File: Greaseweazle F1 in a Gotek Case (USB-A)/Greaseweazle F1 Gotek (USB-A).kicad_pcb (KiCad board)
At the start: 2 copper layers, 111.6 x 68.1 mm, 48 parts, among them CN1 FLOPPY, J1 USB A, J2 Floppy Power, J3 Programming Port, U1 Blue Pill

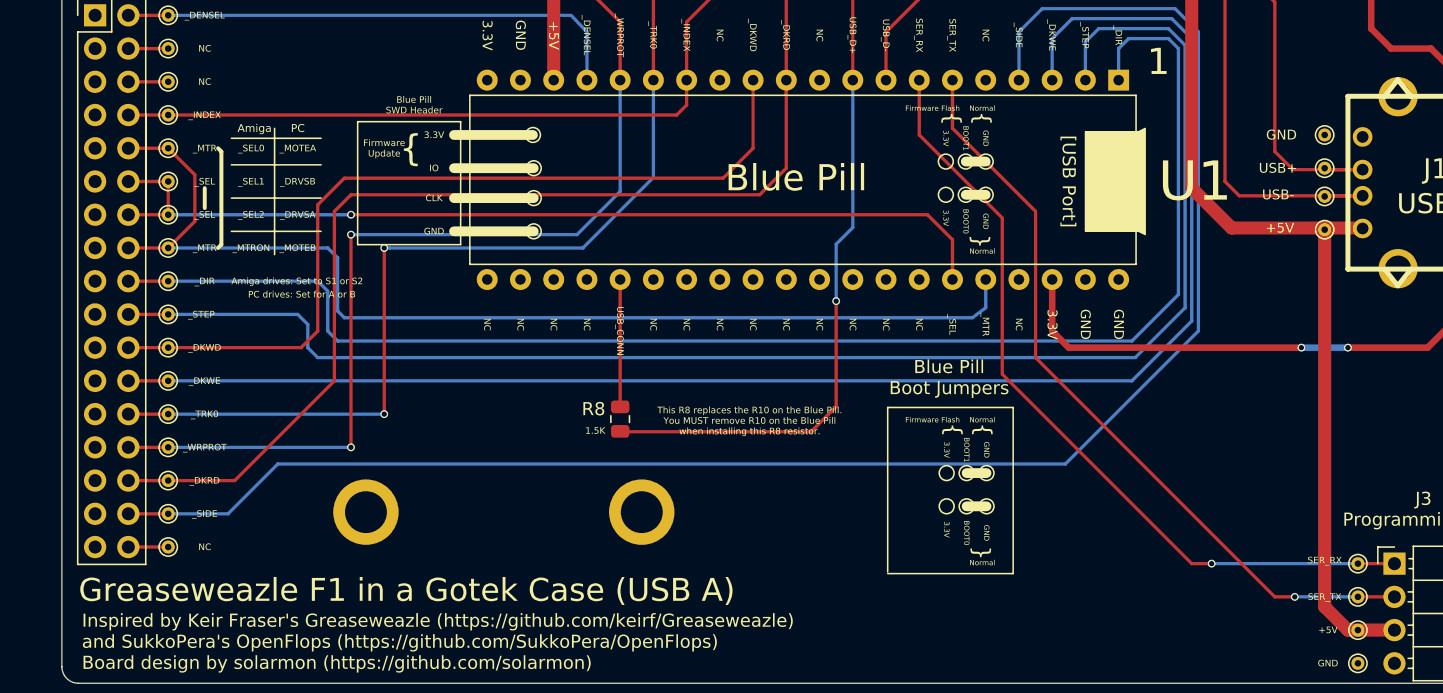
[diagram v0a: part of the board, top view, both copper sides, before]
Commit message: Added internal USB header
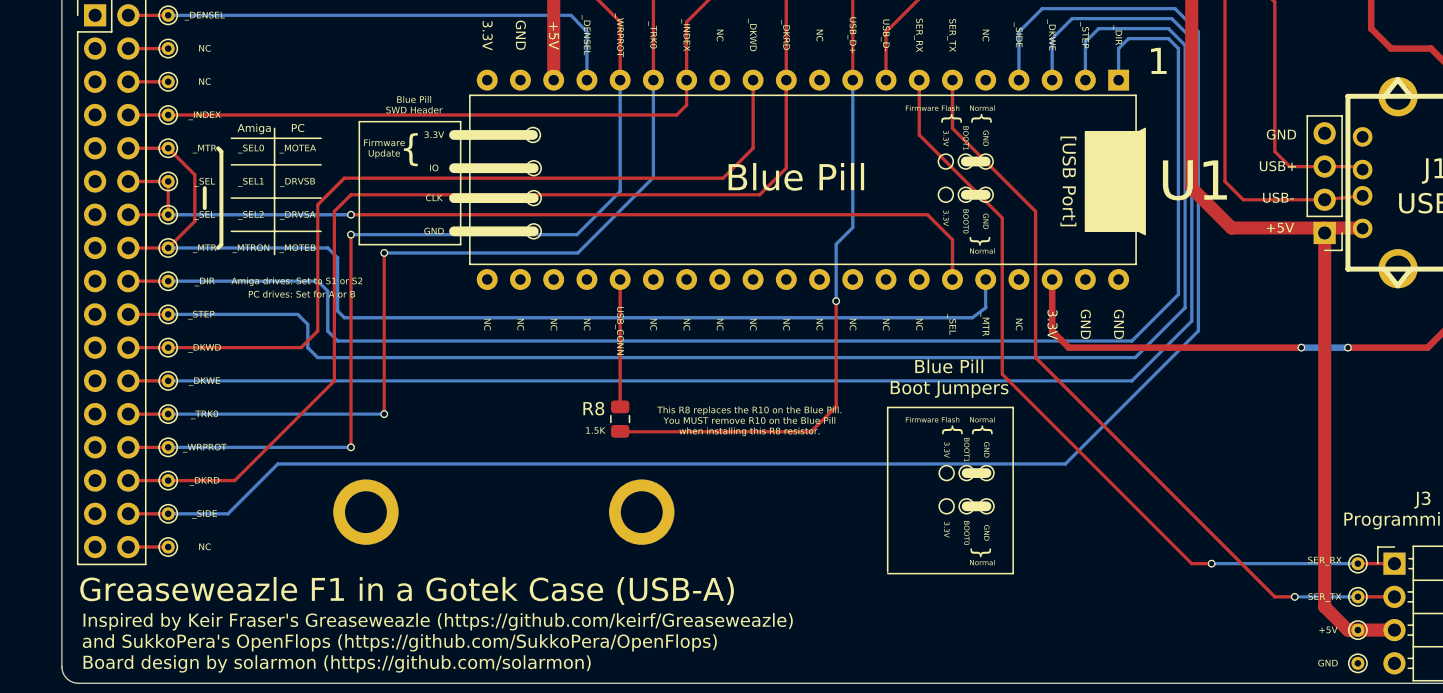
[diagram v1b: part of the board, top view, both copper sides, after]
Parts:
- removed the ? at (191.8, 88.8)
- removed the ? at (191.8, 86.2)
- removed the ? at (191.8, 84.1)
- removed the ? at (191.8, 81.5)
- added ?: PinHeader_1x04_P2.54mm_Vertical, Connector_PinHeader_2.54mm:PinHeader_1x04_P2.54mm_Vertical, F.Cu at (191.8, 89.0)
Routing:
- net Net-(J1-Pad3): track 64.3 -> 61.4 mm
- net Net-(J1-Pad2): track 60.3 -> 57.6 mm
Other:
- board text added: "Greaseweazle F1 in a Gotek Case (USB-A)"
- board text removed: "Greaseweazle F1 in a Gotek Case (USB A)"
